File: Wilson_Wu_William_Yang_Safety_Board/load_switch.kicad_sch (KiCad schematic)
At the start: 20 parts, among them Q3 NTBLS0D8N08XTXG, Q4 NTBLS0D8N08XTXG, U10 LTC4364HS

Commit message: niche
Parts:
- R106: footprint SMV_Passives:0603_resistors -> Library:niche1.5ohmresistor
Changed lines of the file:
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@@
 			)
 		)
-		(property "Footprint" "SMV_Passives:0603_resistors"
+		(property "Footprint" "Library:niche1.5ohmresistor"
 			(at 219.964 57.404 90)
 			(effects

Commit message: layout changes
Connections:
- net at Q3.2, Q3.3, Q3.4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: now also Q3.5, Q3.6, Q3.7, Q3.8, Q4.5, Q4.6, Q4.7, Q4.8; no longer C103.2, Q4.1, R105.1, U10.4 (DGATE), U10.6 (HGATE)
- new net: C103.2, Q4.1, R105.1, U10.4 (DGATE), U10.6 (HGATE)

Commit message: pcb layout
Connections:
- net at C103.2, R105.1, U10.6 (HGATE): no longer Q4.1, U10.4 (DGATE)
- new net: Q4.1, U10.4 (DGATE)
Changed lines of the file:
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@@
-	)
-	(junction
-		(at 166.37 83.82)
-		(diameter 0)
-		(color 0 0 0 0)
 	)
 	(junction
@@
 	(wire
 		(pts
-			(xy 166.37 83.82) (xy 166.37 88.9)
+			(xy 166.37 78.74) (xy 166.37 88.9)
 		)
 		(stroke
@@
 	(wire
 		(pts
-			(xy 139.7 83.82) (xy 166.37 83.82)
-		)
-		(stroke
-			(width 0)
-			(type default)
-		)
-	)
-	(wire
-		(pts
 			(xy 152.4 68.58) (xy 154.94 68.58)
 		)
 		(stroke
-			(width 0)
-			(type default)
-		)
-	)
-	(wire
-		(pts
-			(xy 166.37 78.74) (xy 166.37 83.82)
-		)
-		(stroke

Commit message: layout
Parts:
- added load_switch_tp1, load_switch_tp3: V_DIVIDED, TestPoint:TestPoint_Pad_D1.0mm, symbol Connector:TestPoint
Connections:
- net load switch conn: now also load_switch_tp1.1
- net at Q3.2, Q3.3, Q3.4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: now also load_switch_tp3.1
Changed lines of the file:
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@@
+	)
+	(junction
+		(at 156.21 83.82)
+		(diameter 0)
+		(color 0 0 0 0)
 	)
 	(junction
@@
 	(wire
 		(pts
-			(xy 156.21 66.04) (xy 156.21 91.44)
+			(xy 156.21 66.04) (xy 156.21 83.82)
 		)
 		(stroke
@@
 		(pts
 			(xy 154.94 66.04) (xy 154.94 68.58)
+		)
+		(stroke
+			(width 0)
+			(type default)
+		)
+	)
+	(wire
+		(pts
+			(xy 156.21 83.82) (xy 156.21 91.44)
 		)
 		(stroke
@@
 					(unit 1)
 				)
+			)
+		)
+	)
+	(symbol
+		(lib_id "Connector:TestPoint")
+		(at 156.21 83.82 90)
+		(unit 1)
+		(exclude_from_sim no)
+		(in_bom yes)
+		(on_board yes)
+		(dnp no)
+		(fields_autoplaced yes)
+		(property "Reference" "load_switch_tp3"
+			(at 152.908 81.28 90)
+			(effects
+				(font
+					(size 1.27 1.27)
+				)
+			)
+		)
+		(property "Value" "V_DIVIDED"
+			(at 154.1779 81.28 0)
+			(effects
+				(font
+					(size 1.27 1.27)
+				)
+				(justify left)
+				(hide yes)
+			)
+		)
+		(property "Footprint" "TestPoint:TestPoint_Pad_D1.0mm"
+			(at 156.21 78.74 0)
+			(effects
+				(font
+					(size 1.27 1.27)
+				)
+				(hide yes)
+			)
+		)
+		(property "Datasheet" "~"
+			(at 156.21 78.74 0)
+			(effects
+				(font
+					(size 1.27 1.27)
+				)
+				(hide yes)
+			)
+		)
+		(property "Description" "test point"
+			(at 156.21 83.82 0)
+			(effects
+				(font
+					(size 1.27 1.27)
+				)
+				(hide yes)
+			)
+		)
+		(pin "1"
+		)
+		(instances
+			(project "Wilson_Wu_William_Yang_Safety_Board"
+				(path "/fa857c32-0741-4b91-b122-1a57686bb514/3aab1625-1497-4612-8772-a9d051eba0fa/126bcf17-17b6-4307-9150-bd6ba2c5a143"
+					(reference "load_switch_tp3")
+					(unit 1)
+				)
+			)
+		)
+	)
+	(symbol
+		(lib_id "Connector:TestPoint")
+		(at 88.9 58.42 0)
+		(unit 1)
+		(exclude_from_sim no)
+		(in_bom yes)
+		(on_board yes)
+		(dnp no)
+		(fields_autoplaced yes)
+		(property "Reference" "load_switch_tp1"
+			(at 91.44 55.1179 0)
+			(effects
+				(font
+					(size 1.27 1.27)
+				)
+				(justify left)
+			)
+		)
+		(property "Value" "V_DIVIDED"
+			(at 91.44 56.3879 0)
+			(effects
+				(font
+					(size 1.27 1.27)
+				)
+				(justify left)
+				(hide yes)
+			)
+		)
+		(property "Footprint" "TestPoint:TestPoint_Pad_D1.0mm"
+			(at 93.98 58.42 0)
+			(effects
+				(font
+					(size 1.27 1.27)
+				)
+				(hide yes)
+			)
+		)
+		(property "Datasheet" "~"
+			(at 93.98 58.42 0)
+			(effects
+				(font
+					(size 1.27 1.27)
+				)
+				(hide yes)
+			)
+		)
+		(property "Description" "test point"
+			(at 88.9 58.42 0)
+			(effects
+				(font
+					(size 1.27 1.27)
+				)
+				(hide yes)
+			)
+		)
+		(pin "1"
+		)
+		(instances
+			(project "Wilson_Wu_William_Yang_Safety_Board"
+				(path "/fa857c32-0741-4b91-b122-1a57686bb514/3aab1625-1497-4612-8772-a9d051eba0fa/126bcf17-17b6-4307-9150-bd6ba2c5a143"
+					(reference "load_switch_tp1")
+					(unit 1)
+				)

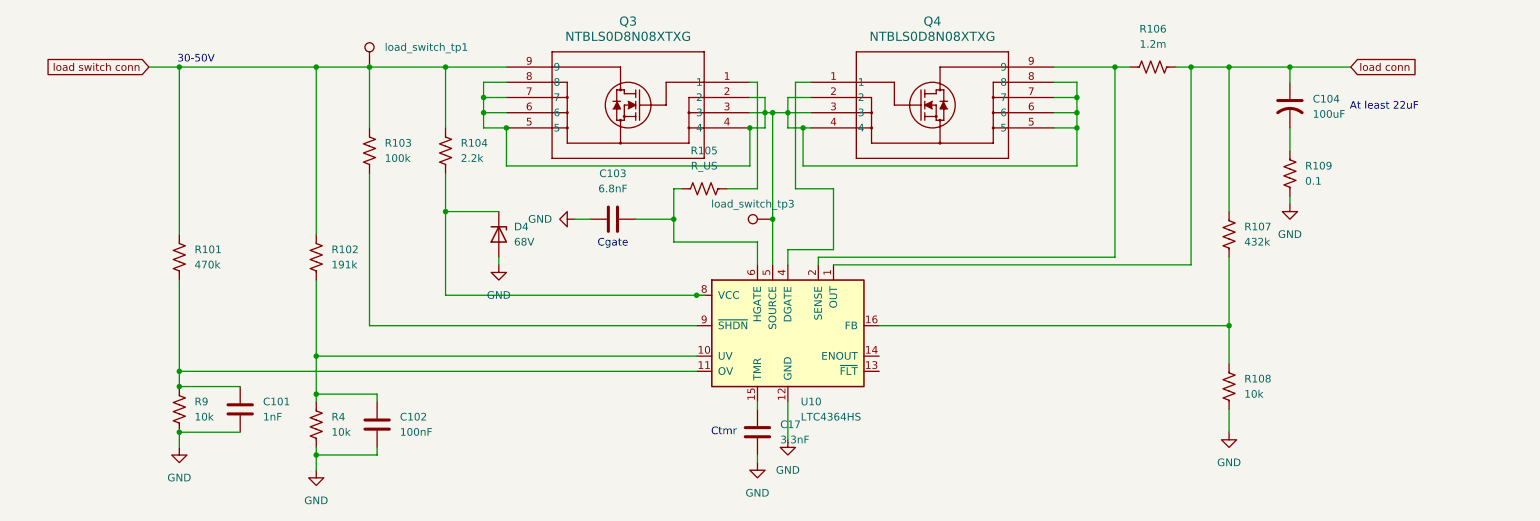
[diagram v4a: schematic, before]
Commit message: layout fixes
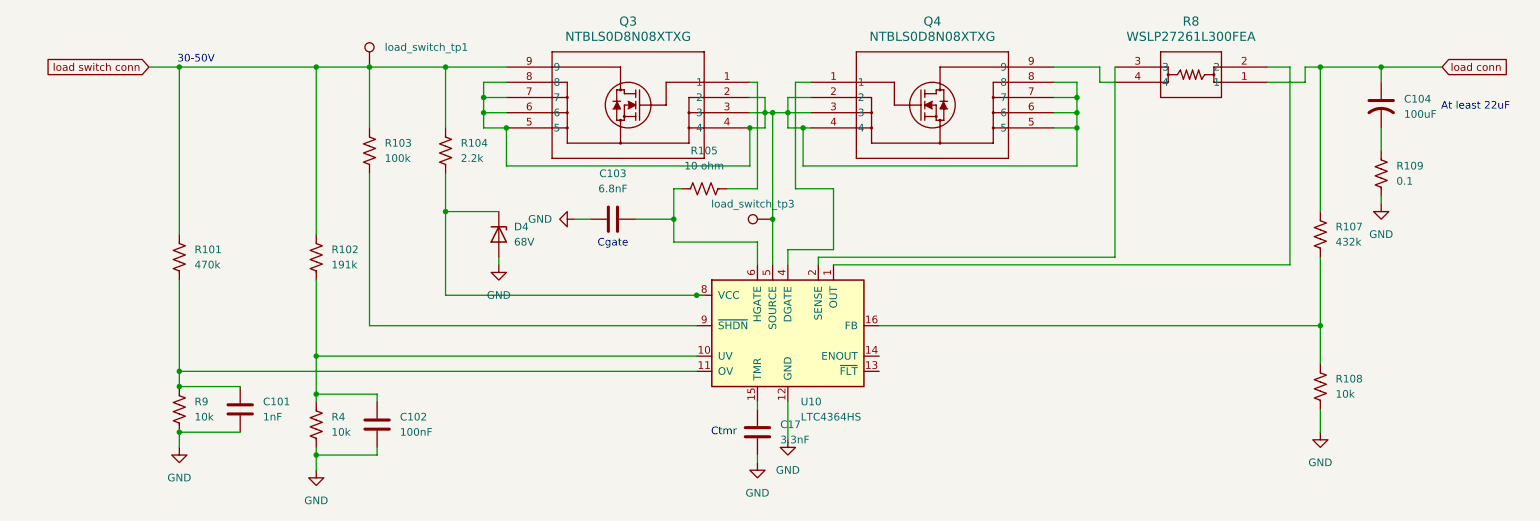
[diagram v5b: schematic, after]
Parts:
- removed R106: 1.2m, Library:niche1.5ohmresistor, symbol Device:R_US
- added R8: WSLP27261L300FEA, WSLP2726_1.3mOHM_VIS, symbol 1.3ohmshunt:WSLP27261L300FEA
- R105: value R_US -> 10 ohm
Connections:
- net load conn: now also R8.1; no longer U10.1 (OUT)
- net at U10.2 (SENSE): now also R8.3; no longer Q4.9
- new net: R8.2, U10.1 (OUT)
- new net: Q4.9, R8.4
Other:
- moved on the sheet: C104, R107, R108, R109

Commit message: changed capacitor footprint and fixed a few drc errors
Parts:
- C104: footprint SMV_Passives:CAPC17595_87N_KEM -> Personal:CAPPRD500W60D1000H2200B
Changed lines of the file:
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@@
 			)
 		)
-		(property "Footprint" "SMV_Passives:CAPC17595_87N_KEM"
+		(property "Footprint" "Personal:CAPPRD500W60D1000H2200B"
 			(at 257.81 64.77 0)
 			(effects

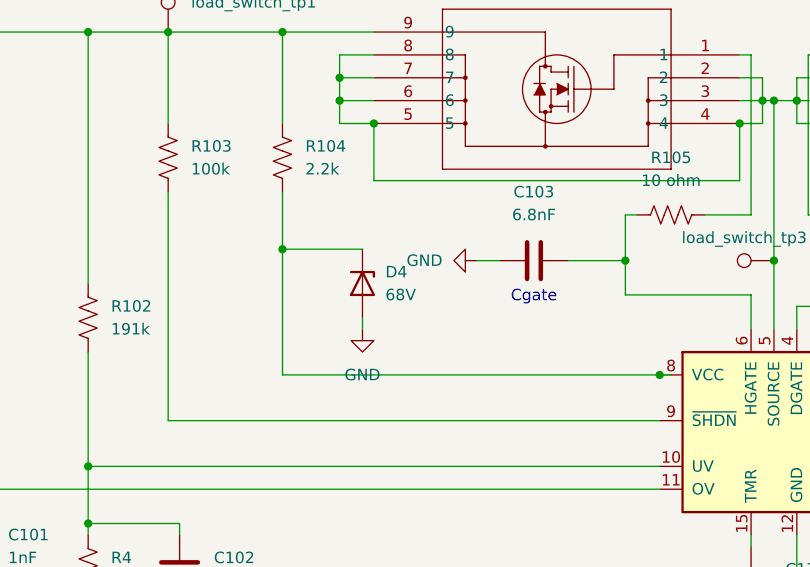
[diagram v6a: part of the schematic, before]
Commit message: changed diode footprint
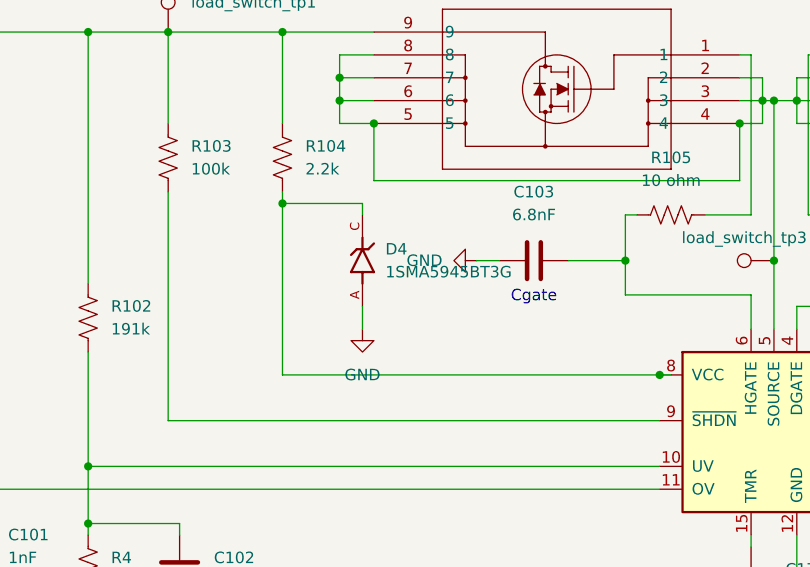
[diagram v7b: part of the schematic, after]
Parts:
- removed D4: 68V, load switch zener diode:P25_DO-214AC_SMA, symbol Device:D_Zener
- added D4: 1SMA5945BT3G, SMV_ICs:DIOM5226X220N, symbol SMV_Custom:1SMA5945BT3G
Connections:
- net GND: now also D4.A
- net at R104.2, U10.8 (VCC): now also D4.C
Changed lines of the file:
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@@
-	)
-	(junction
-		(at 101.6 82.55)
-		(diameter 0)
-		(color 0 0 0 0)
 	)
 	(junction
@@
 	)
 	(junction
+		(at 101.6 77.47)
+		(diameter 0)
+		(color 0 0 0 0)
+	)
+	(junction
 		(at 107.95 63.5)
 		(diameter 0)
@@
 	(wire
 		(pts
-			(xy 101.6 82.55) (xy 101.6 96.52)
+			(xy 101.6 76.2) (xy 101.6 77.47)
 		)
 		(stroke
@@
 	(wire
 		(pts
+			(xy 101.6 77.47) (xy 110.49 77.47)
+		)
+		(stroke
+			(width 0)
+			(type default)
+		)
+	)
+	(wire
+		(pts
 			(xy 152.4 68.58) (xy 152.4 74.93)
 		)
@@
 	(wire
 		(pts
-			(xy 110.49 91.44) (xy 110.49 90.17)
+			(xy 110.49 88.9) (xy 110.49 91.44)
 		)
 		(stroke
@@
 	(wire
 		(pts
+			(xy 110.49 78.74) (xy 110.49 77.47)
+		)
+		(stroke
+			(width 0)
+			(type default)
+		)
+	)
+	(wire
+		(pts
 			(xy 203.2 60.96) (xy 207.01 60.96)
 		)
@@
 	(wire
 		(pts
-			(xy 101.6 76.2) (xy 101.6 82.55)
-		)
-		(stroke
-			(width 0)
-			(type default)
-		)
-	)
-	(wire
-		(pts
 			(xy 203.2 68.58) (xy 207.01 68.58)
 		)
@@
 	(wire
 		(pts
-			(xy 110.49 82.55) (xy 101.6 82.55)
+			(xy 101.6 77.47) (xy 101.6 96.52)
 		)
 		(stroke
@@
 	)
 	(symbol
-		(lib_id "Device:D_Zener")
-		(at 110.49 86.36 270)
-		(unit 1)
-		(exclude_from_sim no)
-		(in_bom yes)
-		(on_board yes)
-		(dnp no)
-		(fields_autoplaced yes)
-		(property "Reference" "D4"
-			(at 113.03 85.0899 90)
-			(effects
-				(font
-					(size 1.27 1.27)
-				)
-				(justify left)
-			)
-		)
-		(property "Value" "68V"
-			(at 113.03 87.6299 90)
-			(effects
-				(font
-					(size 1.27 1.27)
-				)
-				(justify left)
-			)
-		)
-		(property "Footprint" "load switch zener diode:P25_DO-214AC_SMA"
-			(at 110.49 86.36 0)
-			(effects
-				(font
-					(size 1.27 1.27)
-				)
-				(hide yes)
-			)
-		)
-		(property "Datasheet" "~"
-			(at 110.49 86.36 0)
-			(effects
-				(font
-					(size 1.27 1.27)
-				)
-				(hide yes)
-			)
-		)
-		(property "Description" "Zener diode"
-			(at 110.49 86.36 0)
-			(effects
-				(font
-					(size 1.27 1.27)
-				)
-				(hide yes)
-			)
-		)
-		(pin "1"
-		)
-		(pin "2"
-		)
-		(instances
-			(project "Wilson_Wu_William_Yang_Safety_Board"
-				(path "/fa857c32-0741-4b91-b122-1a57686bb514/3aab1625-1497-4612-8772-a9d051eba0fa/126bcf17-17b6-4307-9150-bd6ba2c5a143"
-					(reference "D4")
-					(unit 1)
-				)
-			)
-		)
-	)
-	(symbol
 		(lib_id "power:GND")
 		(at 57.15 121.92 0)
@@
 					(unit 1)
 				)
+			)
+		)
+	)
+	(symbol
+		(lib_id "SMV_Custom:1SMA5945BT3G")
+		(at 110.49 83.82 90)
+		(unit 1)
+		(exclude_from_sim no)
+		(in_bom yes)
+		(on_board yes)
+		(dnp no)
+		(fields_autoplaced yes)
+		(property "Reference" "D4"
+			(at 113.03 82.5499 90)
+			(effects
+				(font
+					(size 1.27 1.27)
+				)
+				(justify right)
+			)
+		)
+		(property "Value" "1SMA5945BT3G"
+			(at 113.03 85.0899 90)
+			(effects
+				(font
+					(size 1.27 1.27)
+				)
+				(justify right)
+			)
+		)
+		(property "Footprint" "SMV_ICs:DIOM5226X220N"
+			(at 110.49 83.82 0)
+			(effects
+				(font
+					(size 1.27 1.27)
+				)
+				(justify bottom)
+				(hide yes)
+			)
+		)
+		(property "Datasheet" ""
+			(at 110.49 83.82 0)
+			(effects
+				(font
+					(size 1.27 1.27)
+				)
+				(hide yes)
+			)
+		)
+		(property "Description" ""
+			(at 110.49 83.82 0)
+			(effects
+				(font
+					(size 1.27 1.27)
+				)
+				(hide yes)
+			)
+		)
+		(property "PARTREV" "10"
+			(at 110.49 83.82 0)
+			(effects
+				(font
+					(size 1.27 1.27)
+				)
+				(justify bottom)
+				(hide yes)
+			)
+		)
+		(property "STANDARD" "IPC-7351B"
+			(at 110.49 83.82 0)
+			(effects
+				(font
+					(size 1.27 1.27)
+				)
+				(justify bottom)
+				(hide yes)
+			)
+		)
+		(property "MAXIMUM_PACKAGE_HEIGHT" "2.20mm"
+			(at 110.49 83.82 0)
+			(effects
+				(font
+					(size 1.27 1.27)
+				)
+				(justify bottom)
+				(hide yes)
+			)
+		)
+		(property "MANUFACTURER" "ON Semiconductor"
+			(at 110.49 83.82 0)
+			(effects
+				(font
+					(size 1.27 1.27)
+				)
+				(justify bottom)
+				(hide yes)
+			)
+		)
+		(pin "A"
+		)
+		(pin "C"
+		)
+		(instances
+			(project ""
+				(path "/fa857c32-0741-4b91-b122-1a57686bb514/3aab1625-1497-4612-8772-a9d051eba0fa/126bcf17-17b6-4307-9150-bd6ba2c5a143"
+					(reference "D4")
+					(unit 1)
+				)
